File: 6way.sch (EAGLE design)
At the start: 19 parts

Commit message: made two more groups of 2, and what fun will I have renaming all the nets...
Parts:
- added PAIR_A_2, PAIR_A_3, PAIR_B_2, PAIR_B_3: (no value), pinhead:PINHD-1X4
- added PAIR_DISCHG_2, PAIR_DISCHG_3: DMG9926, DMG9926:DMG9926
- added PAIR_GD_2, PAIR_GD_3: FAN7385, fan7385:FAN7385
- added PAIR_GD_CBOOT1_2, PAIR_GD_CBOOT1_3, PAIR_GD_CBOOT2_2, PAIR_GD_CBOOT2_3, PAIR_GD_CVDD_2, PAIR_GD_CVDD_3: 0.1uF 25V, microbuilder:CAP_CERAMIC0805
- added PAIR_GD_DBOOT1_2, PAIR_GD_DBOOT1_3, PAIR_GD_DBOOT2_2, PAIR_GD_DBOOT2_3: (no value), microbuilder:DIODESOT23_WIDE
- added PAIR_OPAMP_2, PAIR_OPAMP_3: (no value), microbuilder:LM358
- added RN10, RN11, RN12, RN6, RN7, RN8: (no value), resistor-dil:4R-NCAY16
- added RN5, RN9: 4.7k, resistor-dil:4R-NCAY16
- added SJ10, SJ11, SJ12, SJ5, SJ6, SJ7, SJ8, SJ9: SOLDERJUMPERTRACE, SparkFun-Passives:SOLDERJUMPERTRACE
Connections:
- new net N$10: PAIR_OPAMP_2G$2.+IN, RN8A.1, RN8B.1, RN8D.1
- new net N$11: PAIR_DISCHG_2.G1, PAIR_GD_2.HO1
- new net N$12: PAIR_DISCHG_2.G2, PAIR_GD_2.HO2
- new net N$13: PAIR_OPAMP_3G$1.-IN, RN10A.1, RN10B.1, RN10D.2
- new net N$14: PAIR_OPAMP_3G$1.+IN, RN9A.2, RN9B.2, RN9D.2
- new net N$15: PAIR_OPAMP_3G$2.-IN, RN11A.1, RN11B.1, RN11D.2
- new net N$16: PAIR_OPAMP_3G$2.+IN, RN12A.1, RN12B.1, RN12D.1
- new net N$17: PAIR_DISCHG_3.G1, PAIR_GD_3.HO1
- new net N$18: PAIR_DISCHG_3.G2, PAIR_GD_3.HO2
- new net N$7: PAIR_OPAMP_2G$1.-IN, RN6A.1, RN6B.1, RN6D.2
- new net N$8: PAIR_OPAMP_2G$1.+IN, RN5A.2, RN5B.2, RN5D.2
- new net N$9: PAIR_OPAMP_2G$2.-IN, RN7A.1, RN7B.1, RN7D.2
- new net PAIR_GD_VB1_2: PAIR_GD_2.VB1, PAIR_GD_CBOOT1_2.P$2, PAIR_GD_DBOOT1_2.C
- new net PAIR_GD_VB1_3: PAIR_GD_3.VB1, PAIR_GD_CBOOT1_3.P$2, PAIR_GD_DBOOT1_3.C
- new net PAIR_GD_VB2_2: PAIR_GD_2.VB2, PAIR_GD_CBOOT2_2.P$2, PAIR_GD_DBOOT2_2.C
- new net PAIR_GD_VB2_3: PAIR_GD_3.VB2, PAIR_GD_CBOOT2_3.P$2, PAIR_GD_DBOOT2_3.C
- net +12V: now also PAIR_OPAMP_2G$1.V+, PAIR_OPAMP_3G$1.V+
- net GND: now also PAIR_GD_2.GND, PAIR_GD_3.GND, PAIR_GD_CVDD_2.P$1, PAIR_GD_CVDD_3.P$1, PAIR_OPAMP_2G$1.V-, PAIR_OPAMP_3G$1.V-, RN12D.2, RN5D.1, RN8D.2, RN9D.1
- net PAIR_A+SM_1: now also PAIR_GD_2.VDD, PAIR_GD_3.VDD, PAIR_GD_DBOOT1_2.A, PAIR_GD_DBOOT1_3.A, PAIR_GD_DBOOT2_2.A, PAIR_GD_DBOOT2_3.A, RN5A.1, RN5B.1, RN9A.1, RN9B.1, SJ5.2, SJ9.2
- net PAIR_A+_1: now also PAIR_A_2.1, PAIR_A_3.1, PAIR_DISCHG_2.S1, PAIR_DISCHG_3.S1, PAIR_GD_CVDD_2.P$2, PAIR_GD_CVDD_3.P$2, SJ5.1, SJ9.1
- net PAIR_A-SM_1: now also RN10A.2, RN10B.2, RN6A.2, RN6B.2, SJ10.2, SJ6.2
- net PAIR_A-_1: now also PAIR_A_2.2, PAIR_A_2.3, PAIR_A_3.2, PAIR_A_3.3, SJ10.1, SJ6.1
- net PAIR_A_DISCHG_1: now also PAIR_A_2.4, PAIR_A_3.4, PAIR_DISCHG_2.D1@1, PAIR_DISCHG_2.D1@2, PAIR_DISCHG_3.D1@1, PAIR_DISCHG_3.D1@2, PAIR_GD_2.VS1, PAIR_GD_3.VS1, PAIR_GD_CBOOT1_2.P$1, PAIR_GD_CBOOT1_3.P$1
- net PAIR_A_EN_DISCHG_1: now also PAIR_GD_2.IN1, PAIR_GD_3.IN1
- net PAIR_A_SENSE_1: now also PAIR_OPAMP_2G$1.OUT, PAIR_OPAMP_3G$1.OUT, RN10D.1, RN6D.1
- net PAIR_B+SM_1: now also RN12A.2, RN12B.2, RN8A.2, RN8B.2, SJ11.2, SJ7.2
- net PAIR_B+_1: now also PAIR_B_2.1, PAIR_B_3.1, PAIR_DISCHG_2.S2, PAIR_DISCHG_3.S2, SJ11.1, SJ7.1
- net PAIR_B-SM_1: now also RN11A.2, RN11B.2, RN7A.2, RN7B.2, SJ12.2, SJ8.2
- net PAIR_B-_1: now also PAIR_B_2.2, PAIR_B_2.3, PAIR_B_3.2, PAIR_B_3.3, SJ12.1, SJ8.1
- net PAIR_B_DISCHG_1: now also PAIR_B_2.4, PAIR_B_3.4, PAIR_DISCHG_2.D2@1, PAIR_DISCHG_2.D2@2, PAIR_DISCHG_3.D2@1, PAIR_DISCHG_3.D2@2, PAIR_GD_2.VS2, PAIR_GD_3.VS2, PAIR_GD_CBOOT2_2.P$1, PAIR_GD_CBOOT2_3.P$1
- net PAIR_B_EN_DISCHG_1: now also PAIR_GD_2.IN2, PAIR_GD_3.IN2
- net PAIR_B_SENSE_1: now also PAIR_OPAMP_2G$2.OUT, PAIR_OPAMP_3G$2.OUT, RN11D.1, RN7D.1

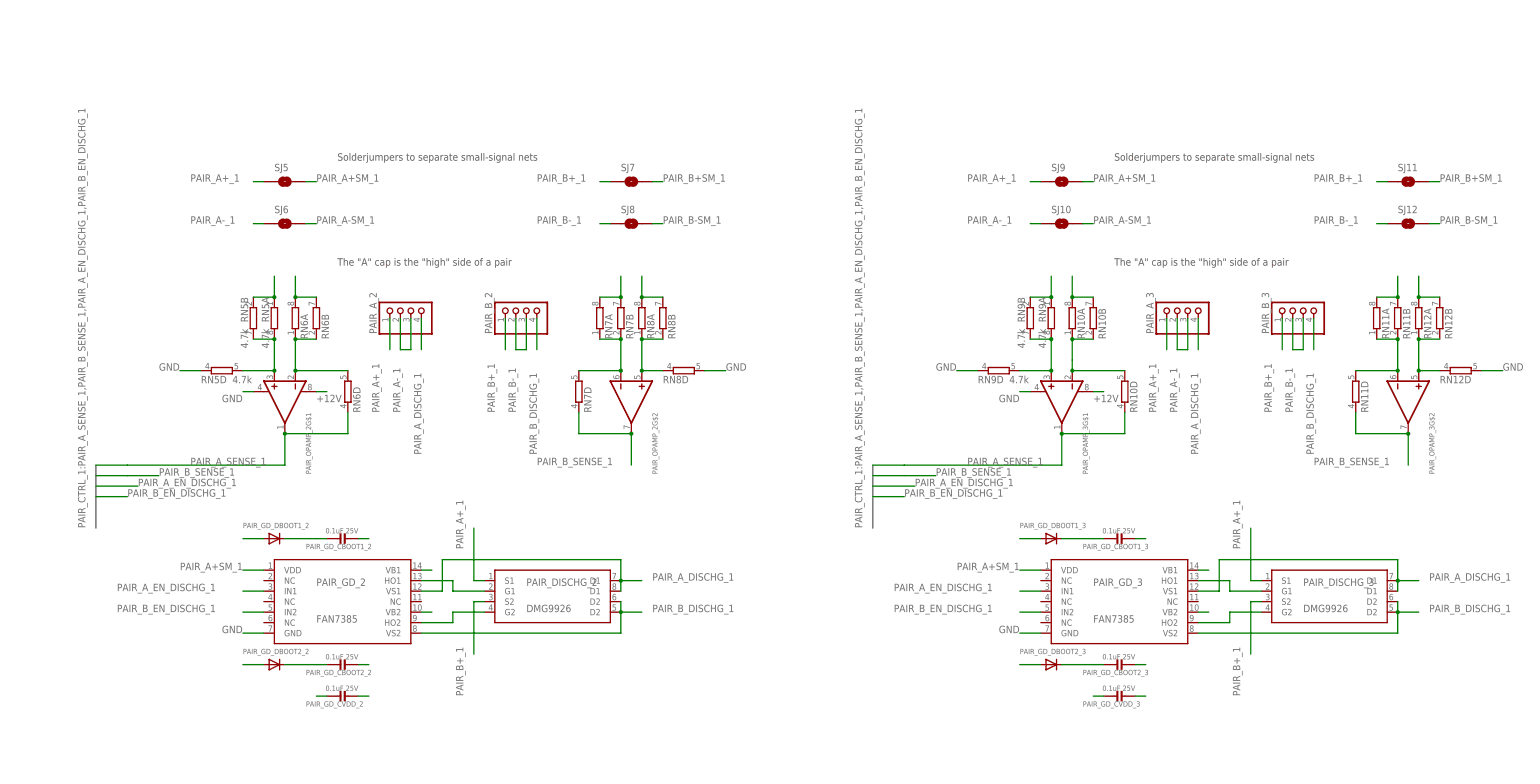
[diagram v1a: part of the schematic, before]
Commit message: removed the other group for now and renamed all the nets in the first copy
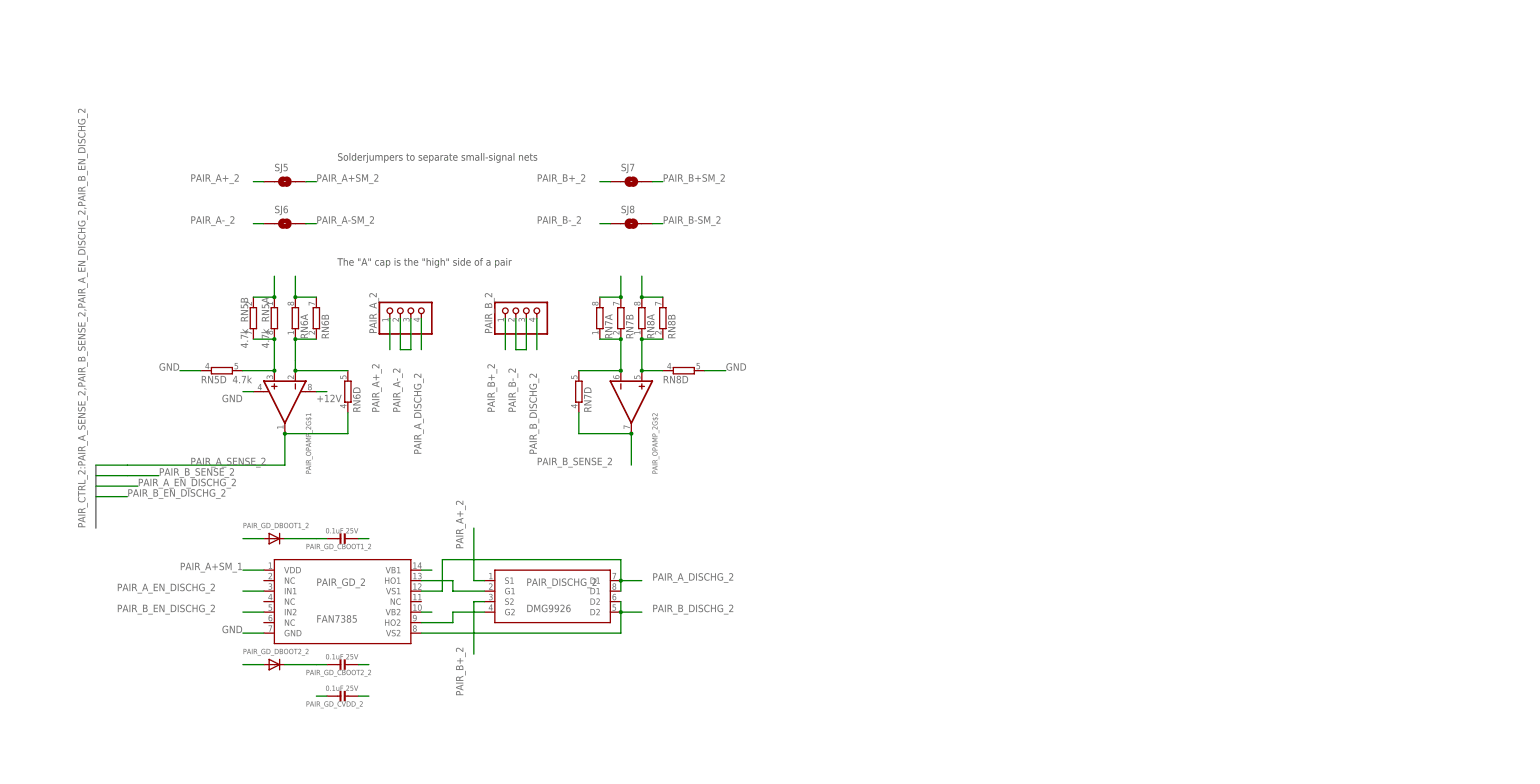
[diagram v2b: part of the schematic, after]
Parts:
- removed PAIR_A_3, PAIR_B_3: (no value), pinhead:PINHD-1X4
- removed PAIR_DISCHG_3: DMG9926, DMG9926:DMG9926
- removed PAIR_GD_3: FAN7385, fan7385:FAN7385
- removed PAIR_GD_CBOOT1_3, PAIR_GD_CBOOT2_3, PAIR_GD_CVDD_3: 0.1uF 25V, microbuilder:CAP_CERAMIC0805
- removed PAIR_GD_DBOOT1_3, PAIR_GD_DBOOT2_3: (no value), microbuilder:DIODESOT23_WIDE
- removed PAIR_OPAMP_3: (no value), microbuilder:LM358
- removed RN10, RN11, RN12: (no value), resistor-dil:4R-NCAY16
- removed RN9: 4.7k, resistor-dil:4R-NCAY16
- removed SJ10, SJ11, SJ12, SJ9: SOLDERJUMPERTRACE, SparkFun-Passives:SOLDERJUMPERTRACE
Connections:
- removed net N$13: PAIR_OPAMP_3G$1.-IN, RN10A.1, RN10B.1, RN10D.2
- removed net N$14: PAIR_OPAMP_3G$1.+IN, RN9A.2, RN9B.2, RN9D.2
- removed net N$15: PAIR_OPAMP_3G$2.-IN, RN11A.1, RN11B.1, RN11D.2
- removed net N$16: PAIR_OPAMP_3G$2.+IN, RN12A.1, RN12B.1, RN12D.1
- removed net N$17: PAIR_DISCHG_3.G1, PAIR_GD_3.HO1
- removed net N$18: PAIR_DISCHG_3.G2, PAIR_GD_3.HO2
- removed net PAIR_GD_VB1_3: PAIR_GD_3.VB1, PAIR_GD_CBOOT1_3.P$2, PAIR_GD_DBOOT1_3.C
- removed net PAIR_GD_VB2_3: PAIR_GD_3.VB2, PAIR_GD_CBOOT2_3.P$2, PAIR_GD_DBOOT2_3.C
- new net PAIR_A+SM_2: PAIR_GD_DBOOT2_2.A, RN5A.1, RN5B.1, SJ5.2
- new net PAIR_A+_2: PAIR_A_2.1, PAIR_DISCHG_2.S1, SJ5.1
- new net PAIR_A-SM_2: RN6A.2, RN6B.2, SJ6.2
- new net PAIR_A-_2: PAIR_A_2.2, PAIR_A_2.3, SJ6.1
- new net PAIR_A_DISCHG_2: PAIR_A_2.4, PAIR_DISCHG_2.D1@1, PAIR_DISCHG_2.D1@2, PAIR_GD_2.VS1, PAIR_GD_CBOOT1_2.P$1
- new net PAIR_A_EN_DISCHG_2: PAIR_GD_2.IN1
- new net PAIR_A_SENSE_2: PAIR_OPAMP_2G$1.OUT, RN6D.1
- new net PAIR_B+SM_2: RN8A.2, RN8B.2, SJ7.2
- new net PAIR_B+_2: PAIR_B_2.1, PAIR_DISCHG_2.S2, SJ7.1
- new net PAIR_B-SM_2: RN7A.2, RN7B.2, SJ8.2
- new net PAIR_B-_2: PAIR_B_2.2, PAIR_B_2.3, SJ8.1
- new net PAIR_B_DISCHG_2: PAIR_B_2.4, PAIR_DISCHG_2.D2@1, PAIR_DISCHG_2.D2@2, PAIR_GD_2.VS2, PAIR_GD_CBOOT2_2.P$1
- new net PAIR_B_EN_DISCHG_2: PAIR_GD_2.IN2
- new net PAIR_B_SENSE_2: PAIR_OPAMP_2G$2.OUT, RN7D.1
- net +12V: no longer PAIR_OPAMP_3G$1.V+
- net GND: no longer PAIR_GD_3.GND, PAIR_GD_CVDD_3.P$1, PAIR_OPAMP_3G$1.V-, RN12D.2, RN9D.1
- net PAIR_A+SM_1: no longer PAIR_GD_3.VDD, PAIR_GD_DBOOT1_3.A, PAIR_GD_DBOOT2_2.A, PAIR_GD_DBOOT2_3.A, RN5A.1, RN5B.1, RN9A.1, RN9B.1, SJ5.2, SJ9.2
- net PAIR_A+_1: no longer PAIR_A_2.1, PAIR_A_3.1, PAIR_DISCHG_2.S1, PAIR_DISCHG_3.S1, PAIR_GD_CVDD_3.P$2, SJ5.1, SJ9.1
- net PAIR_A-SM_1: no longer RN10A.2, RN10B.2, RN6A.2, RN6B.2, SJ10.2, SJ6.2
- net PAIR_A-_1: no longer PAIR_A_2.2, PAIR_A_2.3, PAIR_A_3.2, PAIR_A_3.3, SJ10.1, SJ6.1
- net PAIR_A_DISCHG_1: no longer PAIR_A_2.4, PAIR_A_3.4, PAIR_DISCHG_2.D1@1, PAIR_DISCHG_2.D1@2, PAIR_DISCHG_3.D1@1, PAIR_DISCHG_3.D1@2, PAIR_GD_2.VS1, PAIR_GD_3.VS1, PAIR_GD_CBOOT1_2.P$1, PAIR_GD_CBOOT1_3.P$1
- net PAIR_A_EN_DISCHG_1: no longer PAIR_GD_2.IN1, PAIR_GD_3.IN1
- net PAIR_A_SENSE_1: no longer PAIR_OPAMP_2G$1.OUT, PAIR_OPAMP_3G$1.OUT, RN10D.1, RN6D.1
- net PAIR_B+SM_1: no longer RN12A.2, RN12B.2, RN8A.2, RN8B.2, SJ11.2, SJ7.2
- net PAIR_B+_1: no longer PAIR_B_2.1, PAIR_B_3.1, PAIR_DISCHG_2.S2, PAIR_DISCHG_3.S2, SJ11.1, SJ7.1
- net PAIR_B-SM_1: no longer RN11A.2, RN11B.2, RN7A.2, RN7B.2, SJ12.2, SJ8.2
- net PAIR_B-_1: no longer PAIR_B_2.2, PAIR_B_2.3, PAIR_B_3.2, PAIR_B_3.3, SJ12.1, SJ8.1
- net PAIR_B_DISCHG_1: no longer PAIR_B_2.4, PAIR_B_3.4, PAIR_DISCHG_2.D2@1, PAIR_DISCHG_2.D2@2, PAIR_DISCHG_3.D2@1, PAIR_DISCHG_3.D2@2, PAIR_GD_2.VS2, PAIR_GD_3.VS2, PAIR_GD_CBOOT2_2.P$1, PAIR_GD_CBOOT2_3.P$1
- net PAIR_B_EN_DISCHG_1: no longer PAIR_GD_2.IN2, PAIR_GD_3.IN2
- net PAIR_B_SENSE_1: no longer PAIR_OPAMP_2G$2.OUT, PAIR_OPAMP_3G$2.OUT, RN11D.1, RN7D.1

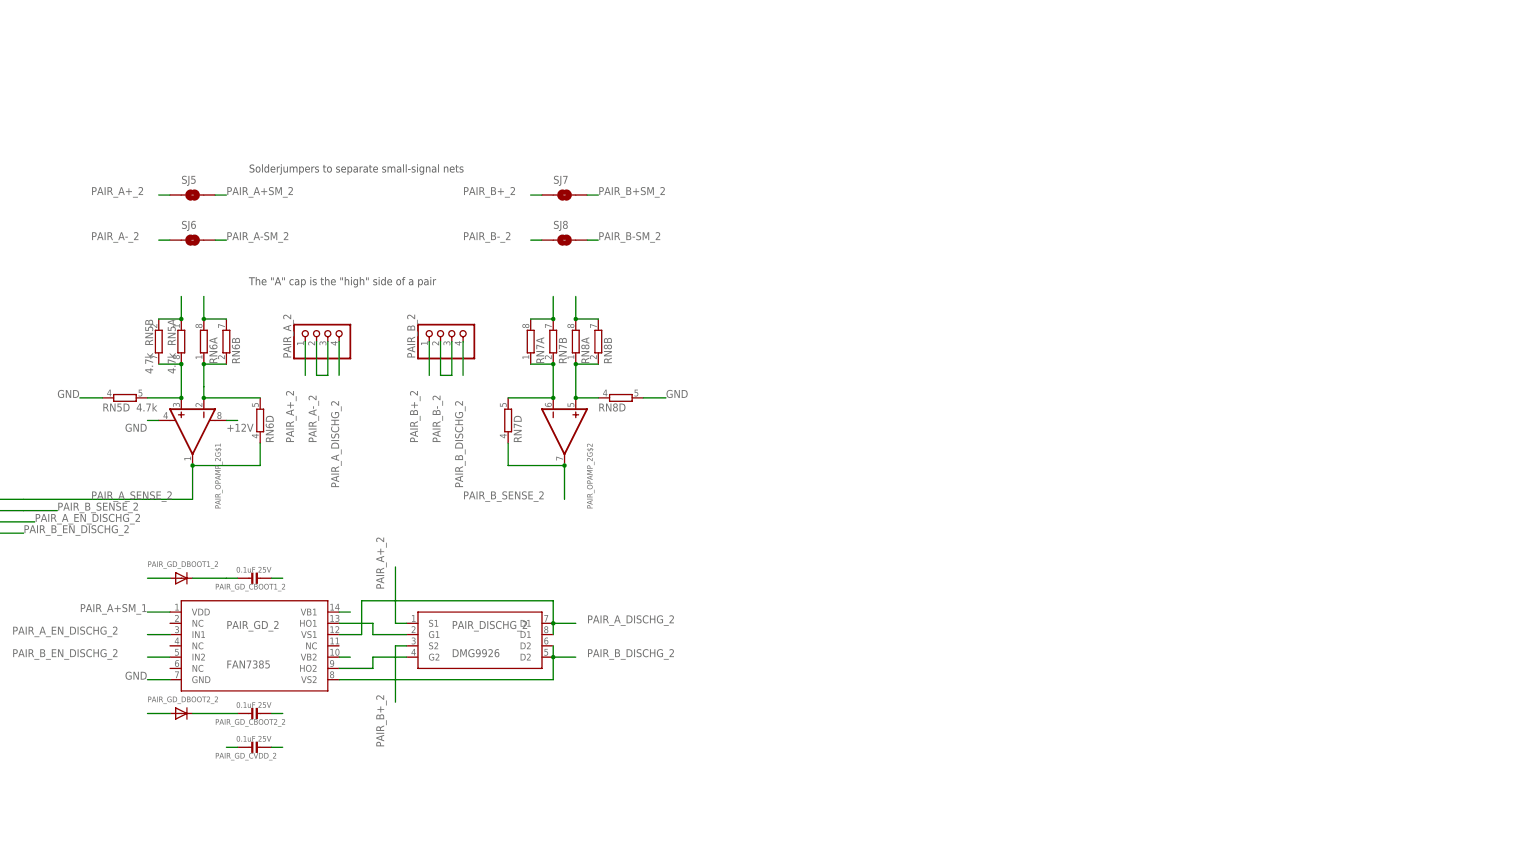
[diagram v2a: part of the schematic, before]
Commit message: third groups renames and a missed small-signal rename
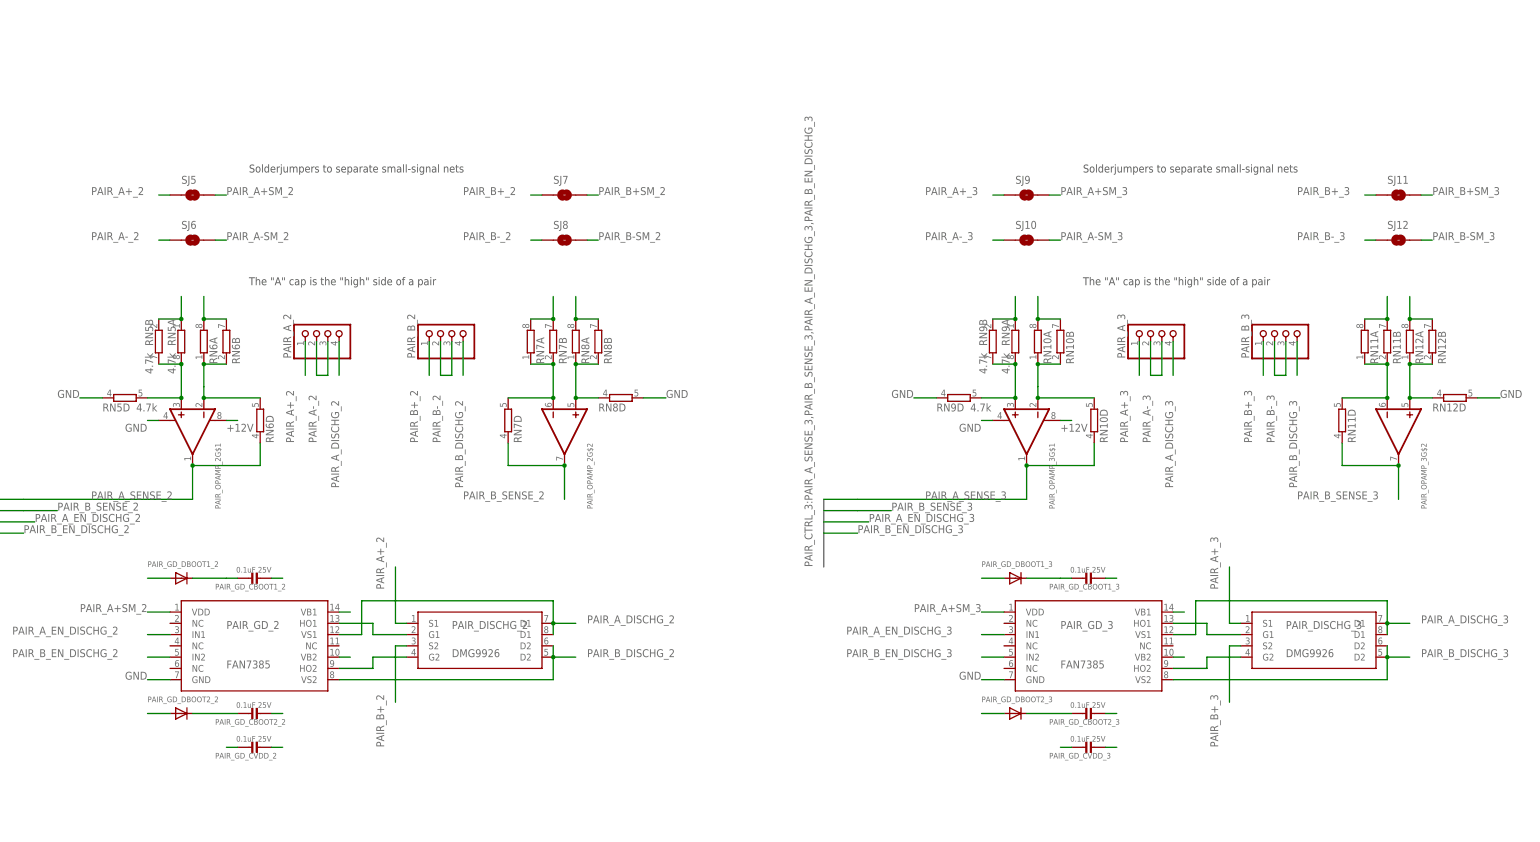
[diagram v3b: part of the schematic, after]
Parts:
- added PAIR_A_3, PAIR_B_3: (no value), pinhead:PINHD-1X4
- added PAIR_DISCHG_3: DMG9926, DMG9926:DMG9926
- added PAIR_GD_3: FAN7385, fan7385:FAN7385
- added PAIR_GD_CBOOT1_3, PAIR_GD_CBOOT2_3, PAIR_GD_CVDD_3: 0.1uF 25V, microbuilder:CAP_CERAMIC0805
- added PAIR_GD_DBOOT1_3, PAIR_GD_DBOOT2_3: (no value), microbuilder:DIODESOT23_WIDE
- added PAIR_OPAMP_3: (no value), microbuilder:LM358
- added RN10, RN11, RN12: (no value), resistor-dil:4R-NCAY16
- added RN9: 4.7k, resistor-dil:4R-NCAY16
- added SJ10, SJ11, SJ12, SJ9: SOLDERJUMPERTRACE, SparkFun-Passives:SOLDERJUMPERTRACE
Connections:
- new net N$13: PAIR_OPAMP_3G$1.-IN, RN10A.1, RN10B.1, RN10D.2
- new net N$14: PAIR_OPAMP_3G$1.+IN, RN9A.2, RN9B.2, RN9D.2
- new net N$15: PAIR_OPAMP_3G$2.-IN, RN11A.1, RN11B.1, RN11D.2
- new net N$16: PAIR_OPAMP_3G$2.+IN, RN12A.1, RN12B.1, RN12D.1
- new net N$17: PAIR_DISCHG_3.G1, PAIR_GD_3.HO1
- new net N$18: PAIR_DISCHG_3.G2, PAIR_GD_3.HO2
- new net PAIR_A+SM_3: PAIR_GD_3.VDD, PAIR_GD_CVDD_3.P$2, PAIR_GD_DBOOT1_3.A, PAIR_GD_DBOOT2_3.A, RN9A.1, RN9B.1, SJ9.2
- new net PAIR_A+_3: PAIR_A_3.1, PAIR_DISCHG_3.S1, SJ9.1
- new net PAIR_A-SM_3: RN10A.2, RN10B.2, SJ10.2
- new net PAIR_A-_3: PAIR_A_3.2, PAIR_A_3.3, SJ10.1
- new net PAIR_A_DISCHG_3: PAIR_A_3.4, PAIR_DISCHG_3.D1@1, PAIR_DISCHG_3.D1@2, PAIR_GD_3.VS1, PAIR_GD_CBOOT1_3.P$1
- new net PAIR_A_EN_DISCHG_3: PAIR_GD_3.IN1
- new net PAIR_A_SENSE_3: PAIR_OPAMP_3G$1.OUT, RN10D.1
- new net PAIR_B+SM_3: RN12A.2, RN12B.2, SJ11.2
- new net PAIR_B+_3: PAIR_B_3.1, PAIR_DISCHG_3.S2, SJ11.1
- new net PAIR_B-SM_3: RN11A.2, RN11B.2, SJ12.2
- new net PAIR_B-_3: PAIR_B_3.2, PAIR_B_3.3, SJ12.1
- new net PAIR_B_DISCHG_3: PAIR_B_3.4, PAIR_DISCHG_3.D2@1, PAIR_DISCHG_3.D2@2, PAIR_GD_3.VS2, PAIR_GD_CBOOT2_3.P$1
- new net PAIR_B_EN_DISCHG_3: PAIR_GD_3.IN2
- new net PAIR_B_SENSE_3: PAIR_OPAMP_3G$2.OUT, RN11D.1
- new net PAIR_GD_VB1_3: PAIR_GD_3.VB1, PAIR_GD_CBOOT1_3.P$2, PAIR_GD_DBOOT1_3.C
- new net PAIR_GD_VB2_3: PAIR_GD_3.VB2, PAIR_GD_CBOOT2_3.P$2, PAIR_GD_DBOOT2_3.C
- net +12V: now also PAIR_OPAMP_3G$1.V+
- net GND: now also PAIR_GD_3.GND, PAIR_GD_CVDD_3.P$1, PAIR_OPAMP_3G$1.V-, RN12D.2, RN9D.1
- net PAIR_A+SM_1: now also PAIR_GD_CVDD_1.P$2; no longer PAIR_GD_2.VDD, PAIR_GD_DBOOT1_2.A
- net PAIR_A+SM_2: now also PAIR_GD_2.VDD, PAIR_GD_CVDD_2.P$2, PAIR_GD_DBOOT1_2.A
- net PAIR_A+_1: no longer PAIR_GD_CVDD_1.P$2, PAIR_GD_CVDD_2.P$2
